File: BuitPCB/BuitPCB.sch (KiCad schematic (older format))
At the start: 3 parts, among them J1 USB_A, J2 RJ45_Abracon_ARJP11A-MASA-B-A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, U1 Teensy4.1

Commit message: Added sheets and connectors
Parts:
- removed J1: USB_A, Connector_USB:USB_A_Stewart_SS-52100-001_Horizontal, symbol Connector:USB_A
- removed J2: RJ45_Abracon_ARJP11A-MASA-B-A-EMU2, Connector_RJ:RJ45_Abracon_ARJP11A-MA_Horizontal, symbol Connector:RJ45_Abracon_ARJP11A-MASA-B-A-EMU2
- removed U1: Teensy4.1, teensy:Teensy41, symbol teensy:Teensy4.1
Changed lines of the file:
@@
 $Descr A4 11693 8268
 encoding utf-8
-Sheet 1 1
+Sheet 1 4
 Title ""
 Date ""
@@
 Comment4 ""
 $EndDescr
-$Comp
-L teensy:Teensy4.1 U1
-U 1 1 61A8F436
-P 6100 4250
-F 0 "U1" H 6100 6815 50  0000 C CNN
-F 1 "Teensy4.1" H 6100 6724 50  0000 C CNN
-F 2 "teensy:Teensy41" H 5700 4650 50  0001 C CNN
-F 3 "" H 5700 4650 50  0001 C CNN
-	1    6100 4250
-	1    0    0    -1
-$EndComp
-$Comp
-L Connector:USB_A J1
-U 1 1 61A96C3A
-P 2600 1950
-F 0 "J1" H 2657 2417 50  0000 C CNN
-F 1 "USB_A" H 2657 2326 50  0000 C CNN
-F 2 "Connector_USB:USB_A_Stewart_SS-52100-001_Horizontal" H 2750 1900 50  0001 C CNN
-F 3 " ~" H 2750 1900 50  0001 C CNN
-	1    2600 1950
-	1    0    0    -1
-$EndComp
-$Comp
-L Connector:RJ45_Abracon_ARJP11A-MASA-B-A-EMU2 J2
-U 1 1 61A99772
-P 9250 2200
-F 0 "J2" H 9250 3717 50  0000 C CNN
-F 1 "RJ45_Abracon_ARJP11A-MASA-B-A-EMU2" H 9250 3626 50  0000 C CNN
-F 2 "Connector_RJ:RJ45_Abracon_ARJP11A-MA_Horizontal" H 9250 3600 50  0001 C CNN
-F 3 "https://abracon.com/Magnetics/lan/ARJP11A.PDF" H 9100 1350 50  0001 C CNN
-	1    9250 2200
-	1    0    0    -1
-$EndComp
+$Sheet
+S 4700 2450 2750 2400
+U 61A90B8E
+F0 "DevBoard" 50
+F1 "DevBoard.sch" 50
+$EndSheet
+$Sheet
+S 8100 1400 2150 1900
+U 61A97DFC
+F0 "Connectivity" 50
+F1 "Connectivity.sch" 50
+$EndSheet
+$Sheet
+S 8050 3900 2150 1750
+U 61AA26AB
+F0 "MIDI" 50
+F1 "MIDI.sch" 50
+$EndSheet
 $EndSCHEMATC

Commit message: Added most of components, few pending
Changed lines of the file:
@@
 $Descr A4 11693 8268
 encoding utf-8
-Sheet 1 4
+Sheet 1 5
 Title ""
 Date ""
@@
 $EndSheet
 $Sheet
-S 8100 1400 2150 1900
-U 61A97DFC
-F0 "Connectivity" 50
-F1 "Connectivity.sch" 50
+S 8200 1500 2150 1750
+U 61AA26AB
+F0 "MIDI&USBhost." 50
+F1 "MIDI&USBhost.sch" 50
 $EndSheet
 $Sheet
-S 8050 3900 2150 1750
-U 61AA26AB
-F0 "MIDI" 50
-F1 "MIDI.sch" 50
+S 1500 2750 2000 1700
+U 61A9E0C1
+F0 "AudioCodec" 50
+F1 "AudioCodec.sch" 50
+$EndSheet
+$Sheet
+S 8200 4100 2050 1550
+U 61AA2264
+F0 "i2cBus&SPI" 50
+F1 "i2cBus&SPI.sch" 50
 $EndSheet
 $EndSCHEMATC

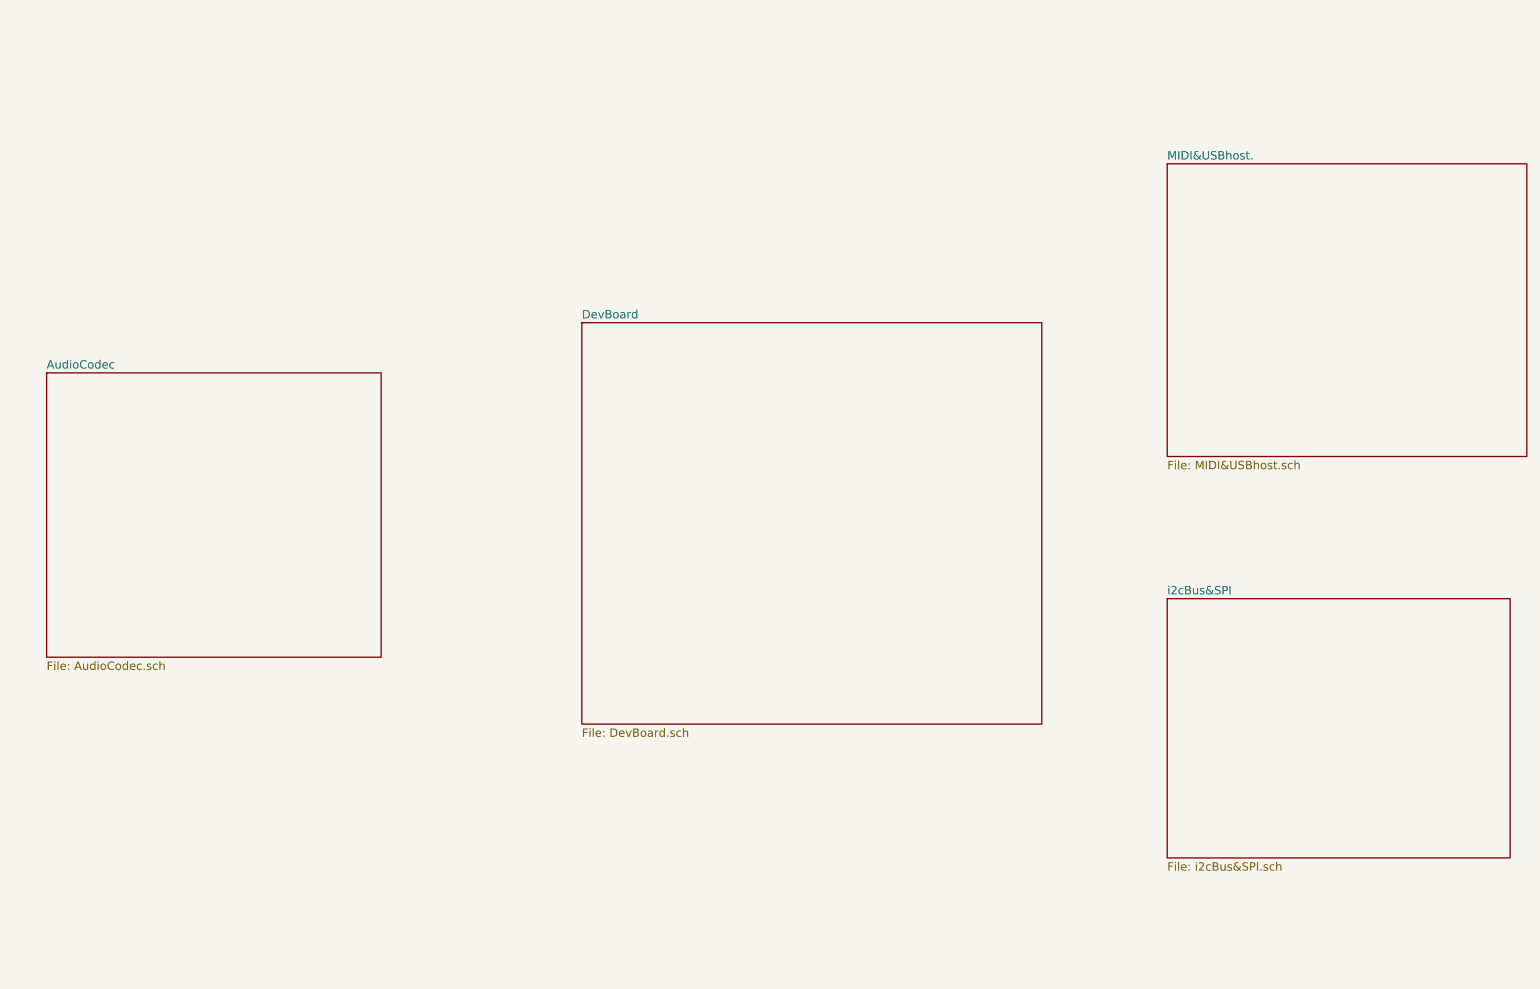
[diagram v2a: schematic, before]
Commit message: Added sensors connectors
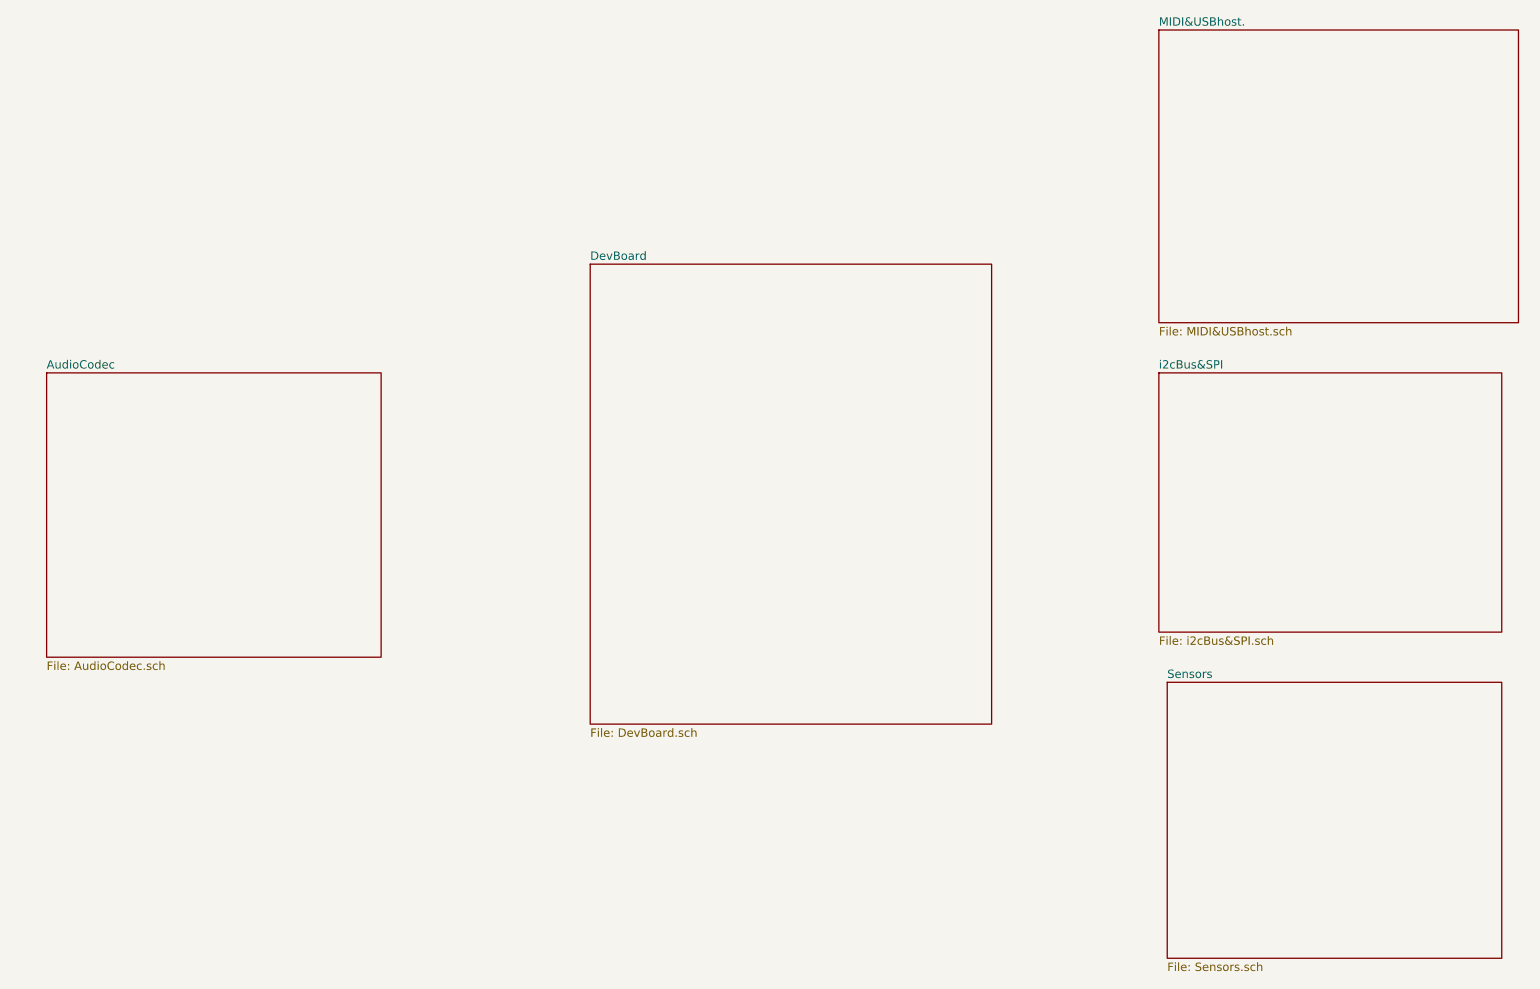
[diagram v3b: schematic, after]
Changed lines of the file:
@@
 $Descr A4 11693 8268
 encoding utf-8
-Sheet 1 5
+Sheet 1 6
 Title ""
 Date ""
@@
 $EndDescr
 $Sheet
-S 4700 2450 2750 2400
+S 4750 2100 2400 2750
 U 61A90B8E
 F0 "DevBoard" 50
@@
 $EndSheet
 $Sheet
-S 8200 1500 2150 1750
+S 8150 700  2150 1750
 U 61AA26AB
 F0 "MIDI&USBhost." 50
@@
 $EndSheet
 $Sheet
-S 8200 4100 2050 1550
+S 8150 2750 2050 1550
 U 61AA2264
 F0 "i2cBus&SPI" 50
 F1 "i2cBus&SPI.sch" 50
 $EndSheet
+$Sheet
+S 8200 4600 2000 1650
+U 61B1CF06
+F0 "Sensors" 50
+F1 "Sensors.sch" 50
+$EndSheet
 $EndSCHEMATC

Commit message: Updated adding battery management sheet and componnents to PCB
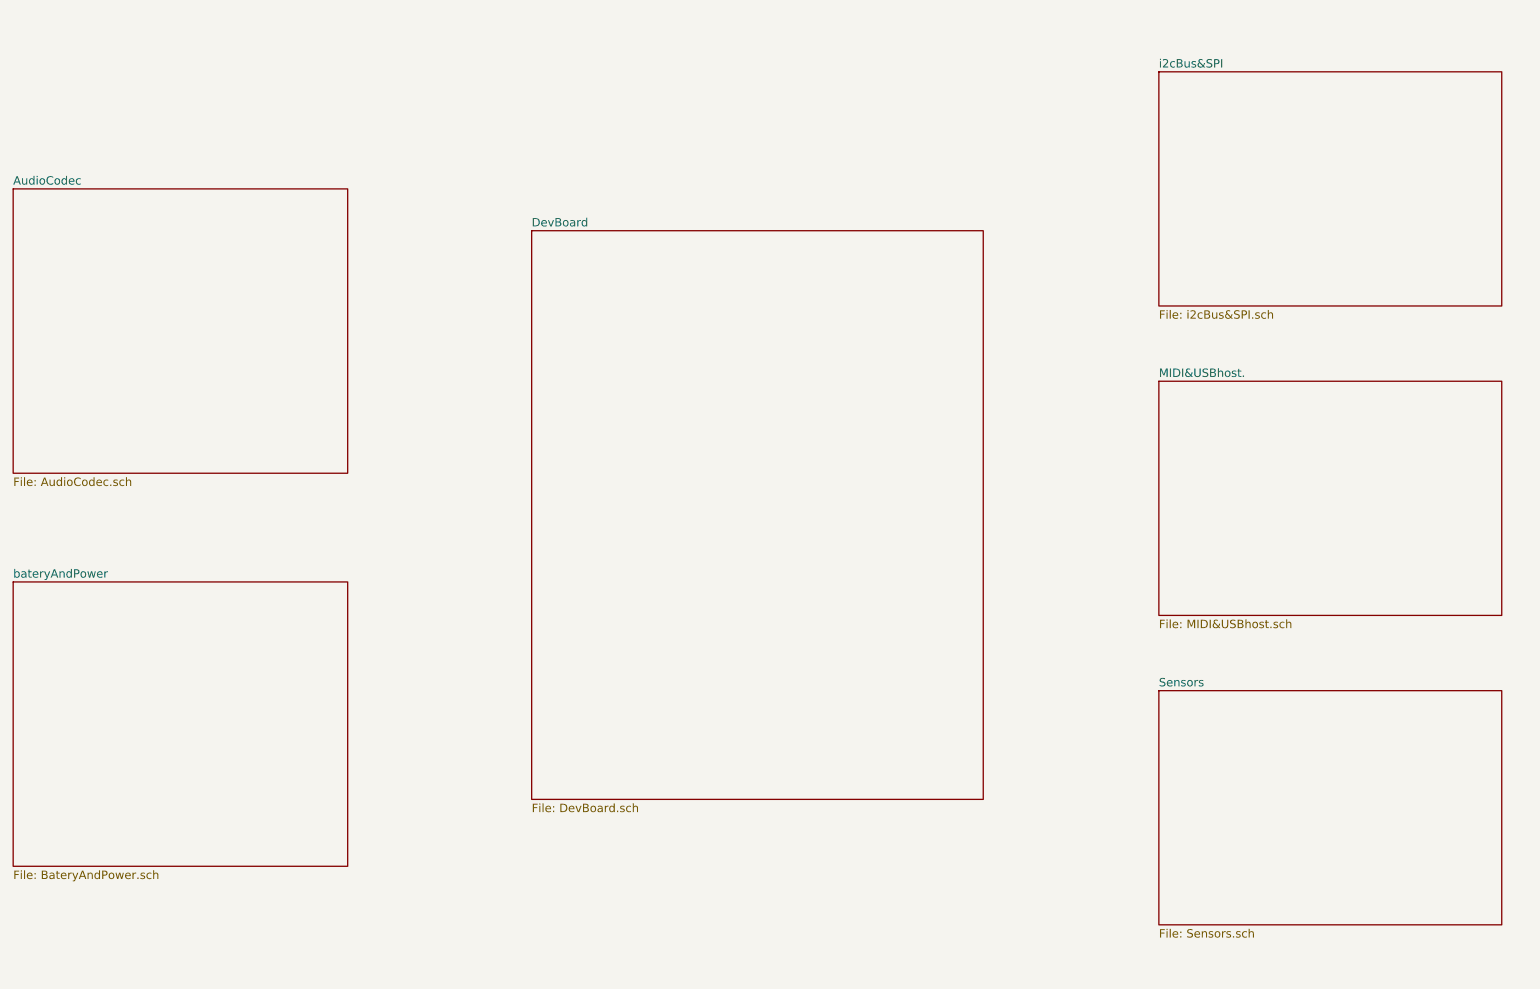
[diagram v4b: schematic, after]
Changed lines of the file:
@@
 $Descr A4 11693 8268
 encoding utf-8
-Sheet 1 6
+Sheet 1 7
 Title ""
 Date ""
@@
 $EndDescr
 $Sheet
-S 4750 2100 2400 2750
+S 4400 1900 2700 3400
 U 61A90B8E
 F0 "DevBoard" 50
@@
 $EndSheet
 $Sheet
-S 8150 700  2150 1750
+S 1300 1650 2000 1700
+U 61A9E0C1
+F0 "AudioCodec" 50
+F1 "AudioCodec.sch" 50
+$EndSheet
+$Sheet
+S 8150 2800 2050 1400
 U 61AA26AB
 F0 "MIDI&USBhost." 50
@@
 $EndSheet
 $Sheet
-S 1500 2750 2000 1700
-U 61A9E0C1
-F0 "AudioCodec" 50
-F1 "AudioCodec.sch" 50
+S 8150 4650 2050 1400
+U 61B1CF06
+F0 "Sensors" 50
+F1 "Sensors.sch" 50
 $EndSheet
 $Sheet
-S 8150 2750 2050 1550
+S 8150 950  2050 1400
 U 61AA2264
 F0 "i2cBus&SPI" 50
@@
 $EndSheet
 $Sheet
-S 8200 4600 2000 1650
-U 61B1CF06
-F0 "Sensors" 50
-F1 "Sensors.sch" 50
+S 1300 4000 2000 1700
+U 61BB14E8
+F0 "bateryAndPower" 50
+F1 "BateryAndPower.sch" 50
 $EndSheet
 $EndSCHEMATC

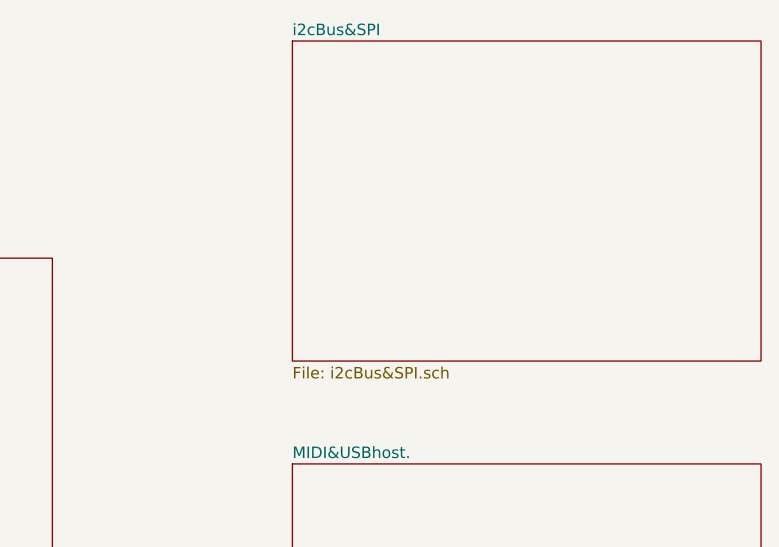
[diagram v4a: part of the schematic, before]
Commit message: Updated to almost every component and started routing
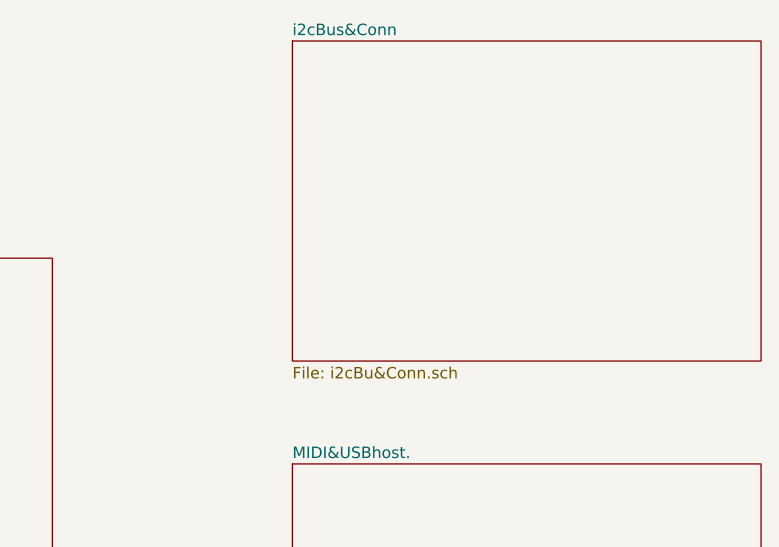
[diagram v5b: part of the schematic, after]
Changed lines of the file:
@@
 S 8150 950  2050 1400
 U 61AA2264
-F0 "i2cBus&SPI" 50
-F1 "i2cBus&SPI.sch" 50
+F0 "i2cBus&Conn" 50
+F1 "i2cBu&Conn.sch" 50
 $EndSheet
 $Sheet
